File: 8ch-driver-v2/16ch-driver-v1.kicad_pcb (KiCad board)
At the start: 4 copper layers, 234 parts, among them J1 Barrel_Jack, J2 Conn_02x16_Odd_Even, Q1 2N7002E, Q10 2N7002E, Q11 2N7002E, Q12 2N7002E, Q13 2N7002E, Q14 2N7002E, Q15 2N7002E, Q16 2N7002E, Q2 2N7002E, Q3 2N7002E, Q4 2N7002E, Q5 2N7002E, Q6 2N7002E, Q7 2N7002E, Q8 2N7002E, Q9 2N7002E, U1 DRV104PWP, U10 DRV104PWP, U11 DRV104PWP, U12 DRV104PWP, U13 DRV104PWP, U14 DRV104PWP, U15 DRV104PWP, U16 DRV104PWP, U17 BD33FC0FP, U18 FT4232H MINI MODULE, U2 DRV104PWP, U3 DRV104PWP, U4 DRV104PWP, U5 DRV104PWP, U6 DRV104PWP, U7 DRV104PWP, U8 DRV104PWP, U9 DRV104PWP

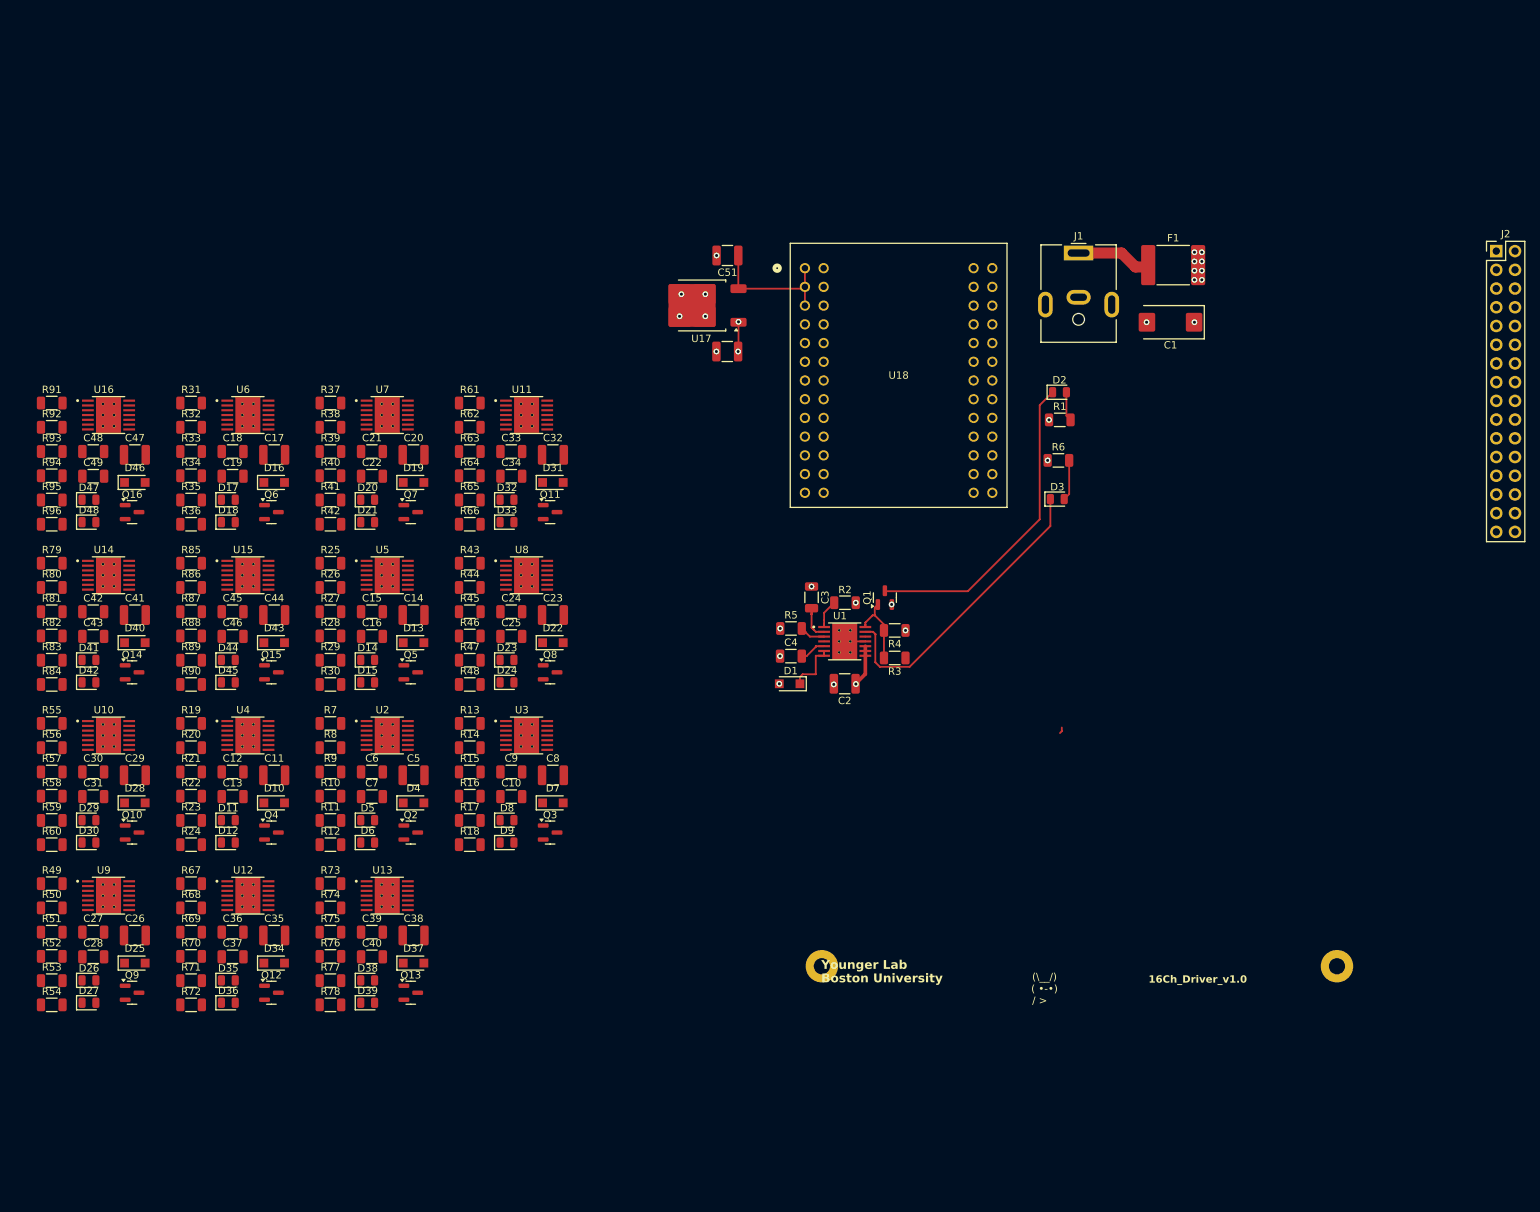
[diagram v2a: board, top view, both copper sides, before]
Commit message: 16-valve PCB layout for inspection
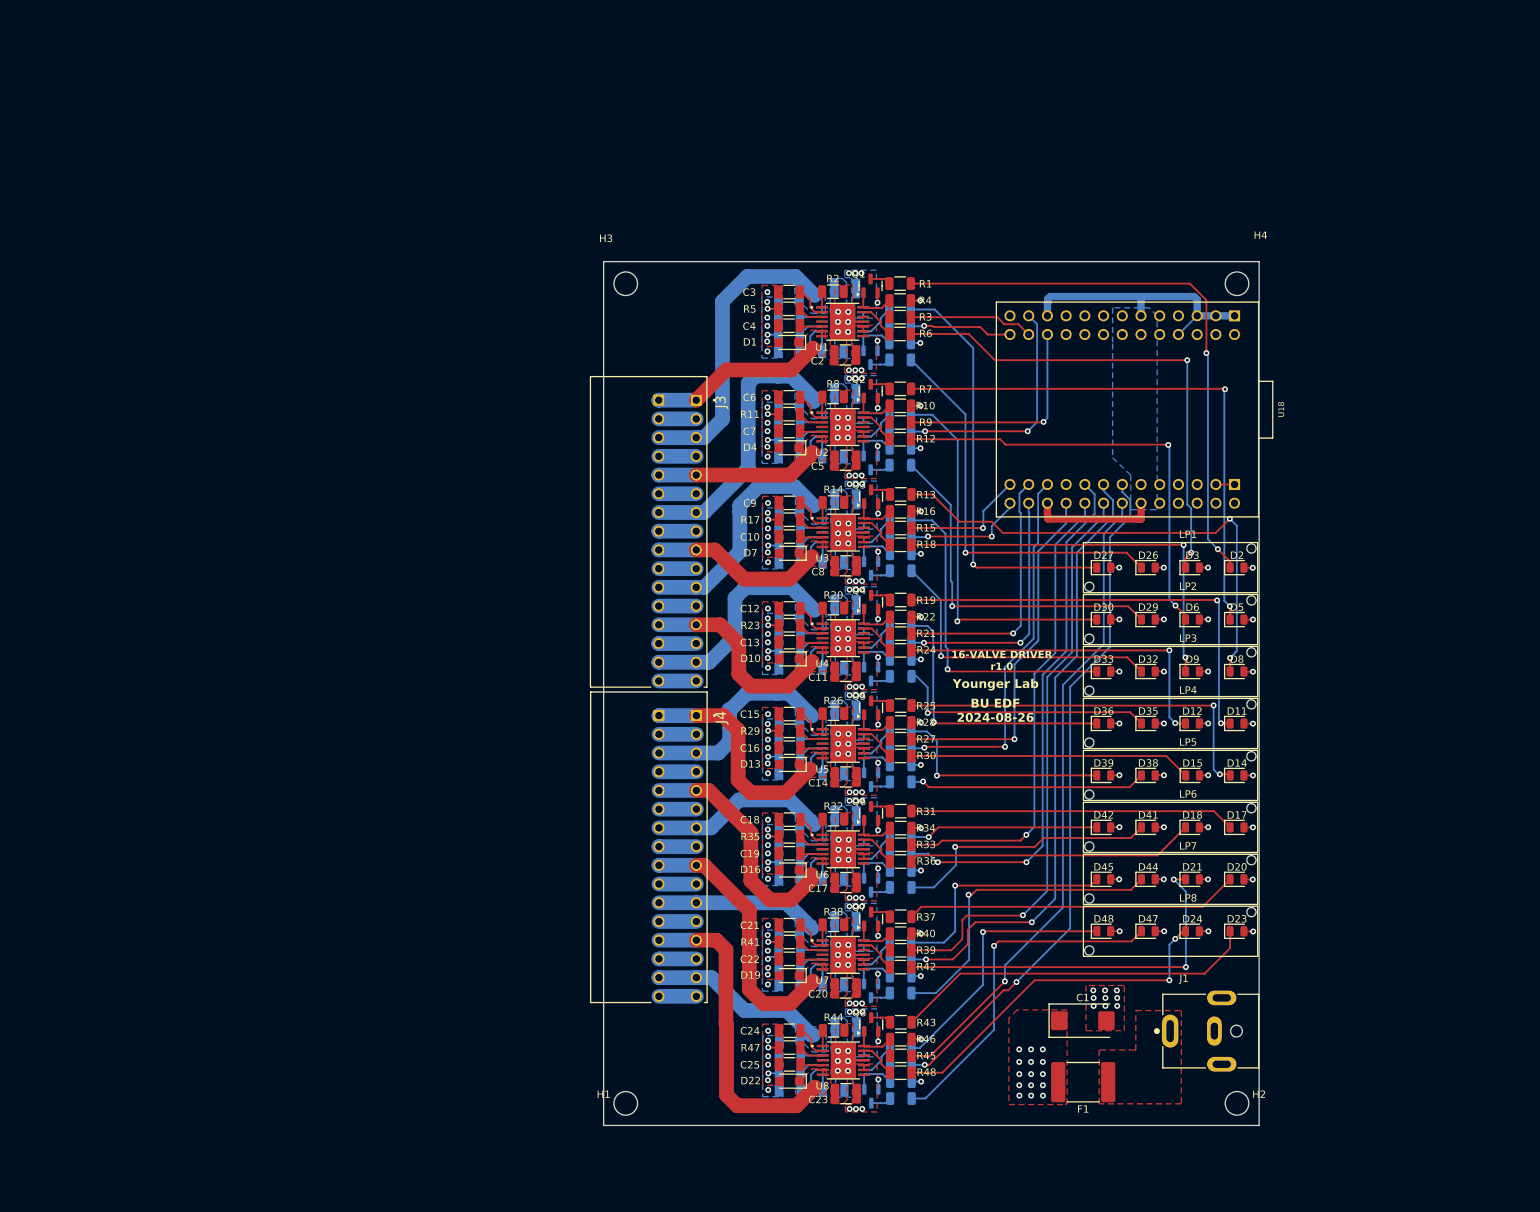
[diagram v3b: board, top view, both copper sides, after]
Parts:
- removed C50, C51: 10uF, Capacitor_SMD:C_1210_3225Metric
- removed J2: Conn_02x16_Odd_Even, Connector_PinHeader_2.54mm:PinHeader_2x16_P2.54mm_Vertical
- removed U17: BD33FC0FP, Package_TO_SOT_SMD:TO-252-2
- added H3: MountingHole, MountingHole:MountingHole_3.2mm_M3, F.Cu at (94.1, 41.8)
- added H4: MountingHole, MountingHole:MountingHole_3.2mm_M3, F.Cu at (183.0, 41.8)
- added J3: TBL009-254-16GY-2GY, footprint:CUI_TBL009-254-16GY-2GY, F.Cu at (106.6, 60.6)
- added J4: TBL009-254-16GY-2GY, footprint:CUI_TBL009-254-16GY-2GY, F.Cu at (106.7, 103.4)
- added LP1: LPF-C014301S, footprint:Lightpipe_LPF-C014301S, F.Cu at (182.7, 83.4)
- added LP2: LPF-C014301S, footprint:Lightpipe_LPF-C014301S, F.Cu at (182.7, 90.4)
- added LP3: LPF-C014301S, footprint:Lightpipe_LPF-C014301S, F.Cu at (182.7, 97.5)
- added LP4: LPF-C014301S, footprint:Lightpipe_LPF-C014301S, F.Cu at (182.7, 104.5)
- added LP5: LPF-C014301S, footprint:Lightpipe_LPF-C014301S, F.Cu at (182.7, 111.6)
- added LP6: LPF-C014301S, footprint:Lightpipe_LPF-C014301S, F.Cu at (182.7, 118.6)
- added LP7: LPF-C014301S, footprint:Lightpipe_LPF-C014301S, F.Cu at (182.7, 125.7)
- added LP8: LPF-C014301S, footprint:Lightpipe_LPF-C014301S, F.Cu at (182.7, 132.7)
- C26, C27, C28, C29, C30, C31, C32, C33, C34, C35, C36, C37, C38, C39, C40, C41, C42, C43, C44, C45, C46, C47, C48, C49, D25, D28, D31, D34, D37, D40, D43, D46, Q10, Q11, Q12, Q13, Q14, Q15, Q16, Q9, R50, R51, R52, R53, R54, R56, R57, R58, R59, R60, R62, R63, R64, R65, R66, R68, R69, R70, R71, R72, R74, R75, R76, R77, R78, R80, R81, R82, R83, R84, R86, R87, R88, R89, R90, R92, R93, R94, R95, R96: moved to B.Cu
- H1, H2: footprint MountingHole:MountingHole_2.2mm_M2_Pad -> MountingHole:MountingHole_3.2mm_M3
- J1: value Barrel_Jack -> PJ-063AH; footprint Connector_BarrelJack:BarrelJack_CUI_PJ-063AH_Horizontal -> footprint:CUI_PJ-063AH
- R1, R13, R19, R25, R31, R37, R43, R7: value 10K -> 4k7
- R49, R55, R61, R67, R73, R79, R85, R91: value 10K -> 4k7; moved to B.Cu
- U1, U2, U3, U4, U5, U6, U7, U8: footprint Solenoid_Driver:IC_TPS27S100BPWPR -> footprint:IC_TPS27S100BPWPR
- U10, U11, U12, U13, U14, U15, U16, U9: footprint Solenoid_Driver:IC_TPS27S100BPWPR -> footprint:IC_TPS27S100BPWPR; moved to B.Cu
- U18: footprint Solenoid_Driver:FT4232H_FTD -> footprint:FT4232H_MINI_MODULE
- moved D47 155.2 mm to (168.0, 132.7)
- moved D26 154.3 mm to (168.0, 83.4)
- moved D27 149.8 mm to (161.9, 83.4)
- moved R91 149.0 mm to (134.4, 155.4), turned to 180 degrees
- moved R54 148.8 mm to (134.3, 48.3), turned to 180 degrees
- moved D48 148.5 mm to (161.9, 132.7)
- moved D29 146.3 mm to (168.0, 90.4)
- moved D41 145.5 mm to (168.0, 118.6)
- moved D17 143.9 mm to (180.0, 118.6)
- moved R93 142.2 mm to (134.4, 150.8), turned to 180 degrees
- moved R52 142.1 mm to (134.3, 52.9), turned to 180 degrees
- moved R94 141.6 mm to (134.4, 153.1), turned to 180 degrees
- moved R51 141.5 mm to (134.3, 50.6), turned to 180 degrees
- moved D30 141.0 mm to (161.9, 90.4)
- moved R92 139.1 mm to (125.3, 154.3), turned to 180 degrees
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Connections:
- net /SpikeAndHoldDriverAndLEDs-1/delay renamed Net-(U1-DELAY_ADJ)
- net /SpikeAndHoldDriverAndLEDs-1/duty renamed Net-(U1-DUTY_CYCLE_ADJ)
- net /SpikeAndHoldDriverAndLEDs-1/freq renamed Net-(U1-OSC_FREQ_ADJ)
- net /SpikeAndHoldDriverAndLEDs-10/delay renamed Net-(U10-DELAY_ADJ)
- net /SpikeAndHoldDriverAndLEDs-10/duty renamed Net-(U10-DUTY_CYCLE_ADJ)
- net /SpikeAndHoldDriverAndLEDs-10/freq renamed Net-(U10-OSC_FREQ_ADJ)
- net /SpikeAndHoldDriverAndLEDs-11/delay renamed Net-(U11-DELAY_ADJ)
- net /SpikeAndHoldDriverAndLEDs-11/duty renamed Net-(U11-DUTY_CYCLE_ADJ)
- net /SpikeAndHoldDriverAndLEDs-11/freq renamed Net-(U11-OSC_FREQ_ADJ)
- net /SpikeAndHoldDriverAndLEDs-12/delay renamed Net-(U12-DELAY_ADJ)
- net /SpikeAndHoldDriverAndLEDs-12/duty renamed Net-(U12-DUTY_CYCLE_ADJ)
- net /SpikeAndHoldDriverAndLEDs-12/freq renamed Net-(U12-OSC_FREQ_ADJ)
- net /SpikeAndHoldDriverAndLEDs-13/delay renamed Net-(U13-DELAY_ADJ)
- net /SpikeAndHoldDriverAndLEDs-13/duty renamed Net-(U13-DUTY_CYCLE_ADJ)
- net /SpikeAndHoldDriverAndLEDs-13/freq renamed Net-(U13-OSC_FREQ_ADJ)
- net /SpikeAndHoldDriverAndLEDs-14/delay renamed Net-(U14-DELAY_ADJ)
- net /SpikeAndHoldDriverAndLEDs-14/duty renamed Net-(U14-DUTY_CYCLE_ADJ)
- net /SpikeAndHoldDriverAndLEDs-14/freq renamed Net-(U14-OSC_FREQ_ADJ)
- net /SpikeAndHoldDriverAndLEDs-15/delay renamed Net-(U15-DELAY_ADJ)
- net /SpikeAndHoldDriverAndLEDs-15/duty renamed Net-(U15-DUTY_CYCLE_ADJ)
- net /SpikeAndHoldDriverAndLEDs-15/freq renamed Net-(U15-OSC_FREQ_ADJ)
- net /SpikeAndHoldDriverAndLEDs-16/delay renamed Net-(U16-DELAY_ADJ)
- net /SpikeAndHoldDriverAndLEDs-16/duty renamed Net-(U16-DUTY_CYCLE_ADJ)
- net /SpikeAndHoldDriverAndLEDs-16/freq renamed Net-(U16-OSC_FREQ_ADJ)
- net /SpikeAndHoldDriverAndLEDs-2/delay renamed Net-(U2-DELAY_ADJ)
- net /SpikeAndHoldDriverAndLEDs-2/duty renamed Net-(U2-DUTY_CYCLE_ADJ)
- net /SpikeAndHoldDriverAndLEDs-2/freq renamed Net-(U2-OSC_FREQ_ADJ)
- net /SpikeAndHoldDriverAndLEDs-3/delay renamed Net-(U3-DELAY_ADJ)
- net /SpikeAndHoldDriverAndLEDs-3/duty renamed Net-(U3-DUTY_CYCLE_ADJ)
- net /SpikeAndHoldDriverAndLEDs-3/freq renamed Net-(U3-OSC_FREQ_ADJ)
- net /SpikeAndHoldDriverAndLEDs-4/delay renamed Net-(U4-DELAY_ADJ)
- net /SpikeAndHoldDriverAndLEDs-4/duty renamed Net-(U4-DUTY_CYCLE_ADJ)
- net /SpikeAndHoldDriverAndLEDs-4/freq renamed Net-(U4-OSC_FREQ_ADJ)
- net /SpikeAndHoldDriverAndLEDs-5/delay renamed Net-(U5-DELAY_ADJ)
- net /SpikeAndHoldDriverAndLEDs-5/duty renamed Net-(U5-DUTY_CYCLE_ADJ)
- net /SpikeAndHoldDriverAndLEDs-5/freq renamed Net-(U5-OSC_FREQ_ADJ)
- net /SpikeAndHoldDriverAndLEDs-6/delay renamed Net-(U6-DELAY_ADJ)
- net /SpikeAndHoldDriverAndLEDs-6/duty renamed Net-(U6-DUTY_CYCLE_ADJ)
- net /SpikeAndHoldDriverAndLEDs-6/freq renamed Net-(U6-OSC_FREQ_ADJ)
- net /SpikeAndHoldDriverAndLEDs-7/delay renamed Net-(U7-DELAY_ADJ)
- net /SpikeAndHoldDriverAndLEDs-7/duty renamed Net-(U7-DUTY_CYCLE_ADJ)
- net /SpikeAndHoldDriverAndLEDs-7/freq renamed Net-(U7-OSC_FREQ_ADJ)
- net /SpikeAndHoldDriverAndLEDs-8/delay renamed Net-(U8-DELAY_ADJ)
- net /SpikeAndHoldDriverAndLEDs-8/duty renamed Net-(U8-DUTY_CYCLE_ADJ)
- net /SpikeAndHoldDriverAndLEDs-8/freq renamed Net-(U8-OSC_FREQ_ADJ)
- net /SpikeAndHoldDriverAndLEDs-9/delay renamed Net-(U9-DELAY_ADJ)
- net /SpikeAndHoldDriverAndLEDs-9/duty renamed Net-(U9-DUTY_CYCLE_ADJ)
- net /SpikeAndHoldDriverAndLEDs-9/freq renamed Net-(U9-OSC_FREQ_ADJ)
- D11 pad 2: Net-(D11-A) -> +12V
- D12 pad 1: /SpikeAndHoldDriverAndLEDs-4/fault -> Net-(D12-K)
- D12 pad 2: Net-(D12-A) -> +12V
- D14 pad 2: Net-(D14-A) -> +12V
- D15 pad 1: /SpikeAndHoldDriverAndLEDs-5/fault -> Net-(D15-K)
- D15 pad 2: Net-(D15-A) -> +12V
- D17 pad 2: Net-(D17-A) -> +12V
- D18 pad 1: /SpikeAndHoldDriverAndLEDs-6/fault -> Net-(D18-K)
- D18 pad 2: Net-(D18-A) -> +12V
- D2 pad 2: Net-(D2-A) -> +12V
- D20 pad 2: Net-(D20-A) -> +12V
- D21 pad 1: /SpikeAndHoldDriverAndLEDs-7/fault -> Net-(D21-K)
- D21 pad 2: Net-(D21-A) -> +12V
- D23 pad 2: Net-(D23-A) -> +12V
- D24 pad 1: /SpikeAndHoldDriverAndLEDs-8/fault -> Net-(D24-K)
- D24 pad 2: Net-(D24-A) -> +12V
- D26 pad 2: Net-(D26-A) -> +12V
- D27 pad 1: /SpikeAndHoldDriverAndLEDs-9/fault -> Net-(D27-K)
- D27 pad 2: Net-(D27-A) -> +12V
- D29 pad 2: Net-(D29-A) -> +12V
- D3 pad 1: /SpikeAndHoldDriverAndLEDs-1/fault -> Net-(D3-K)
- D3 pad 2: Net-(D3-A) -> +12V
- D30 pad 1: /SpikeAndHoldDriverAndLEDs-10/fault -> Net-(D30-K)
- D30 pad 2: Net-(D30-A) -> +12V
- D32 pad 2: Net-(D32-A) -> +12V
- D33 pad 1: /SpikeAndHoldDriverAndLEDs-11/fault -> Net-(D33-K)
- D33 pad 2: Net-(D33-A) -> +12V
- D35 pad 2: Net-(D35-A) -> +12V
- D36 pad 1: /SpikeAndHoldDriverAndLEDs-12/fault -> Net-(D36-K)
- D36 pad 2: Net-(D36-A) -> +12V
- D38 pad 2: Net-(D38-A) -> +12V
- D39 pad 1: /SpikeAndHoldDriverAndLEDs-13/fault -> Net-(D39-K)
- D39 pad 2: Net-(D39-A) -> +12V
- D41 pad 2: Net-(D41-A) -> +12V
- D42 pad 1: /SpikeAndHoldDriverAndLEDs-14/fault -> Net-(D42-K)
- D42 pad 2: Net-(D42-A) -> +12V
- D44 pad 2: Net-(D44-A) -> +12V
- D45 pad 1: /SpikeAndHoldDriverAndLEDs-15/fault -> Net-(D45-K)
- D45 pad 2: Net-(D45-A) -> +12V
- D47 pad 2: Net-(D47-A) -> +12V
- D48 pad 1: /SpikeAndHoldDriverAndLEDs-16/fault -> Net-(D48-K)
- D48 pad 2: Net-(D48-A) -> +12V
- D5 pad 2: Net-(D5-A) -> +12V
- D6 pad 1: /SpikeAndHoldDriverAndLEDs-2/fault -> Net-(D6-K)
- D6 pad 2: Net-(D6-A) -> +12V
- D8 pad 2: Net-(D8-A) -> +12V
- D9 pad 1: /SpikeAndHoldDriverAndLEDs-3/fault -> Net-(D9-K)
- D9 pad 2: Net-(D9-A) -> +12V
- Q1 pad 3: Net-(D2-K) -> Net-(Q1-D)
- Q10 pad 3: Net-(D29-K) -> Net-(Q10-D)
- Q11 pad 3: Net-(D32-K) -> Net-(Q11-D)
- Q12 pad 3: Net-(D35-K) -> Net-(Q12-D)
- Q13 pad 3: Net-(D38-K) -> Net-(Q13-D)
- Q14 pad 3: Net-(D41-K) -> Net-(Q14-D)
- Q15 pad 3: Net-(D44-K) -> Net-(Q15-D)
- Q16 pad 3: Net-(D47-K) -> Net-(Q16-D)
- Q2 pad 3: Net-(D5-K) -> Net-(Q2-D)
- Q3 pad 3: Net-(D8-K) -> Net-(Q3-D)
- Q4 pad 3: Net-(D11-K) -> Net-(Q4-D)
- Q5 pad 3: Net-(D14-K) -> Net-(Q5-D)
- Q6 pad 3: Net-(D17-K) -> Net-(Q6-D)
- Q7 pad 3: Net-(D20-K) -> Net-(Q7-D)
- Q8 pad 3: Net-(D23-K) -> Net-(Q8-D)
- Q9 pad 3: Net-(D26-K) -> Net-(Q9-D)
- R1 pad 1: +12V -> Net-(D2-K)
- R1 pad 2: Net-(D2-A) -> Net-(Q1-D)
- R12 pad 1: +12V -> Net-(D6-K)
- R12 pad 2: Net-(D6-A) -> Net-(U2-STATUS_OK_FLAG)
- R13 pad 1: +12V -> Net-(D8-K)
- R13 pad 2: Net-(D8-A) -> Net-(Q3-D)
- R18 pad 1: +12V -> Net-(D9-K)
- R18 pad 2: Net-(D9-A) -> Net-(U3-STATUS_OK_FLAG)
- R19 pad 1: +12V -> Net-(D11-K)
- R19 pad 2: Net-(D11-A) -> Net-(Q4-D)
- R24 pad 1: +12V -> Net-(D12-K)
- R24 pad 2: Net-(D12-A) -> Net-(U4-STATUS_OK_FLAG)
- R25 pad 1: +12V -> Net-(D14-K)
- R25 pad 2: Net-(D14-A) -> Net-(Q5-D)
- R30 pad 1: +12V -> Net-(D15-K)
- R30 pad 2: Net-(D15-A) -> Net-(U5-STATUS_OK_FLAG)
- R31 pad 1: +12V -> Net-(D17-K)
- R31 pad 2: Net-(D17-A) -> Net-(Q6-D)
- R36 pad 1: +12V -> Net-(D18-K)
- R36 pad 2: Net-(D18-A) -> Net-(U6-STATUS_OK_FLAG)
- R37 pad 1: +12V -> Net-(D20-K)
- R37 pad 2: Net-(D20-A) -> Net-(Q7-D)
- R42 pad 1: +12V -> Net-(D21-K)
- R42 pad 2: Net-(D21-A) -> Net-(U7-STATUS_OK_FLAG)
- R43 pad 1: +12V -> Net-(D23-K)
- R43 pad 2: Net-(D23-A) -> Net-(Q8-D)
- R48 pad 1: +12V -> Net-(D24-K)
- R48 pad 2: Net-(D24-A) -> Net-(U8-STATUS_OK_FLAG)
- R49 pad 1: +12V -> Net-(D26-K)
- R49 pad 2: Net-(D26-A) -> Net-(Q9-D)
- R54 pad 1: +12V -> Net-(D27-K)
- R54 pad 2: Net-(D27-A) -> Net-(U9-STATUS_OK_FLAG)
- R55 pad 1: +12V -> Net-(D29-K)
- R55 pad 2: Net-(D29-A) -> Net-(Q10-D)
- R6 pad 1: +12V -> Net-(D3-K)
- R6 pad 2: Net-(D3-A) -> Net-(U1-STATUS_OK_FLAG)
- R60 pad 1: +12V -> Net-(D30-K)
- R60 pad 2: Net-(D30-A) -> Net-(U10-STATUS_OK_FLAG)
- R61 pad 1: +12V -> Net-(D32-K)
- R61 pad 2: Net-(D32-A) -> Net-(Q11-D)
- R66 pad 1: +12V -> Net-(D33-K)
- R66 pad 2: Net-(D33-A) -> Net-(U11-STATUS_OK_FLAG)
- R67 pad 1: +12V -> Net-(D35-K)
- R67 pad 2: Net-(D35-A) -> Net-(Q12-D)
- R7 pad 1: +12V -> Net-(D5-K)
- R7 pad 2: Net-(D5-A) -> Net-(Q2-D)
- R72 pad 1: +12V -> Net-(D36-K)
- R72 pad 2: Net-(D36-A) -> Net-(U12-STATUS_OK_FLAG)
- R73 pad 1: +12V -> Net-(D38-K)
- R73 pad 2: Net-(D38-A) -> Net-(Q13-D)
- R78 pad 1: +12V -> Net-(D39-K)
- R78 pad 2: Net-(D39-A) -> Net-(U13-STATUS_OK_FLAG)
- R79 pad 1: +12V -> Net-(D41-K)
- R79 pad 2: Net-(D41-A) -> Net-(Q14-D)
- R84 pad 1: +12V -> Net-(D42-K)
- R84 pad 2: Net-(D42-A) -> Net-(U14-STATUS_OK_FLAG)
- R85 pad 1: +12V -> Net-(D44-K)
- R85 pad 2: Net-(D44-A) -> Net-(Q15-D)
- R90 pad 1: +12V -> Net-(D45-K)
- R90 pad 2: Net-(D45-A) -> Net-(U15-STATUS_OK_FLAG)
- R91 pad 1: +12V -> Net-(D47-K)
- R91 pad 2: Net-(D47-A) -> Net-(Q16-D)
- R96 pad 1: +12V -> Net-(D48-K)
- R96 pad 2: Net-(D48-A) -> Net-(U16-STATUS_OK_FLAG)
- U1 pad 13: /SpikeAndHoldDriverAndLEDs-1/fault -> Net-(U1-STATUS_OK_FLAG)
- U10 pad 13: /SpikeAndHoldDriverAndLEDs-10/fault -> Net-(U10-STATUS_OK_FLAG)
- U11 pad 13: /SpikeAndHoldDriverAndLEDs-11/fault -> Net-(U11-STATUS_OK_FLAG)
- U12 pad 13: /SpikeAndHoldDriverAndLEDs-12/fault -> Net-(U12-STATUS_OK_FLAG)
- U13 pad 13: /SpikeAndHoldDriverAndLEDs-13/fault -> Net-(U13-STATUS_OK_FLAG)
- U14 pad 13: /SpikeAndHoldDriverAndLEDs-14/fault -> Net-(U14-STATUS_OK_FLAG)
- U15 pad 13: /SpikeAndHoldDriverAndLEDs-15/fault -> Net-(U15-STATUS_OK_FLAG)
- U16 pad 13: /SpikeAndHoldDriverAndLEDs-16/fault -> Net-(U16-STATUS_OK_FLAG)
- U18 pad CN2-10: /SpikeAndHoldDriverAndLEDs-2/TTLInput -> unconnected-(U18-AD1-PadCN2-10)
- U18 pad CN2-11: unconnected-(U18-VIO-PadCN2-11) -> +3.3V
- U18 pad CN2-12: /SpikeAndHoldDriverAndLEDs-4/TTLInput -> unconnected-(U18-AD3-PadCN2-12)
- U18 pad CN2-13: /SpikeAndHoldDriverAndLEDs-6/TTLInput -> unconnected-(U18-AD5-PadCN2-13)
- U18 pad CN2-14: /SpikeAndHoldDriverAndLEDs-5/TTLInput -> unconnected-(U18-AD4-PadCN2-14)
- U18 pad CN2-15: /SpikeAndHoldDriverAndLEDs-8/TTLInput -> unconnected-(U18-AD7-PadCN2-15)
- U18 pad CN2-16: /SpikeAndHoldDriverAndLEDs-7/TTLInput -> unconnected-(U18-AD6-PadCN2-16)
- U18 pad CN2-21: unconnected-(U18-VIO-PadCN2-21) -> +3.3V
- U18 pad CN2-22: unconnected-(U18-BD4-PadCN2-22) -> /SpikeAndHoldDriverAndLEDs-2/TTLInput
- U18 pad CN2-23: unconnected-(U18-BD6-PadCN2-23) -> /SpikeAndHoldDriverAndLEDs-10/TTLInput
- U18 pad CN2-24: unconnected-(U18-BD5-PadCN2-24) -> /SpikeAndHoldDriverAndLEDs-1/TTLInput
- U18 pad CN2-26: unconnected-(U18-BD7-PadCN2-26) -> /SpikeAndHoldDriverAndLEDs-9/TTLInput
- U18 pad CN2-7: /SpikeAndHoldDriverAndLEDs-1/TTLInput -> unconnected-(U18-AD0-PadCN2-7)
- U18 pad CN2-8: unconnected-(U18-RESET#-PadCN2-8) -> +3.3V
- U18 pad CN2-9: /SpikeAndHoldDriverAndLEDs-3/TTLInput -> unconnected-(U18-AD2-PadCN2-9)
- U18 pad CN3-12: unconnected-(U18-VIO-PadCN3-12) -> +3.3V
- U18 pad CN3-13: unconnected-(U18-DD4-PadCN3-13) -> /SpikeAndHoldDriverAndLEDs-16/TTLInput
- U18 pad CN3-14: unconnected-(U18-DD3-PadCN3-14) -> /SpikeAndHoldDriverAndLEDs-8/TTLInput
- U18 pad CN3-15: unconnected-(U18-DD2-PadCN3-15) -> /SpikeAndHoldDriverAndLEDs-15/TTLInput
- U18 pad CN3-16: unconnected-(U18-DD1-PadCN3-16) -> /SpikeAndHoldDriverAndLEDs-7/TTLInput
- U18 pad CN3-17: unconnected-(U18-DD0-PadCN3-17) -> /SpikeAndHoldDriverAndLEDs-14/TTLInput
- U18 pad CN3-18: /SpikeAndHoldDriverAndLEDs-16/TTLInput -> /SpikeAndHoldDriverAndLEDs-6/TTLInput
- U18 pad CN3-19: /SpikeAndHoldDriverAndLEDs-15/TTLInput -> unconnected-(U18-CD6-PadCN3-19)
- U18 pad CN3-20: /SpikeAndHoldDriverAndLEDs-14/TTLInput -> /SpikeAndHoldDriverAndLEDs-5/TTLInput
- U18 pad CN3-22: unconnected-(U18-VIO-PadCN3-22) -> +3.3V
- U18 pad CN3-23: /SpikeAndHoldDriverAndLEDs-12/TTLInput -> /SpikeAndHoldDriverAndLEDs-4/TTLInput
- U18 pad CN3-24: /SpikeAndHoldDriverAndLEDs-11/TTLInput -> /SpikeAndHoldDriverAndLEDs-12/TTLInput
- U18 pad CN3-25: /SpikeAndHoldDriverAndLEDs-10/TTLInput -> /SpikeAndHoldDriverAndLEDs-3/TTLInput
- U18 pad CN3-26: /SpikeAndHoldDriverAndLEDs-9/TTLInput -> /SpikeAndHoldDriverAndLEDs-11/TTLInput
- U2 pad 13: /SpikeAndHoldDriverAndLEDs-2/fault -> Net-(U2-STATUS_OK_FLAG)
- U3 pad 13: /SpikeAndHoldDriverAndLEDs-3/fault -> Net-(U3-STATUS_OK_FLAG)
- U4 pad 13: /SpikeAndHoldDriverAndLEDs-4/fault -> Net-(U4-STATUS_OK_FLAG)
- U5 pad 13: /SpikeAndHoldDriverAndLEDs-5/fault -> Net-(U5-STATUS_OK_FLAG)
- U6 pad 13: /SpikeAndHoldDriverAndLEDs-6/fault -> Net-(U6-STATUS_OK_FLAG)
- U7 pad 13: /SpikeAndHoldDriverAndLEDs-7/fault -> Net-(U7-STATUS_OK_FLAG)
- U8 pad 13: /SpikeAndHoldDriverAndLEDs-8/fault -> Net-(U8-STATUS_OK_FLAG)
- U9 pad 13: /SpikeAndHoldDriverAndLEDs-9/fault -> Net-(U9-STATUS_OK_FLAG)
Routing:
- net GND: track 2.94 -> 179.1 mm, vias 15 -> 153
- net /SpikeAndHoldDriverAndLEDs-16/TTLInput: track 0.00 -> 93.2 mm, vias 0 -> 2
- net /SpikeAndHoldDriverAndLEDs-8/TTLInput: track 0.00 -> 88.3 mm, vias 0 -> 1
- net /SpikeAndHoldDriverAndLEDs-15/TTLInput: track 0.00 -> 84.2 mm, vias 0 -> 2
- net /SpikeAndHoldDriverAndLEDs-7/TTLInput: track 0.00 -> 79.1 mm, vias 0 -> 1
- net Net-(D5-K): track 0.00 -> 74.2 mm, vias 0 -> 2
- net /SpikeAndHoldDriverAndLEDs-14/TTLInput: track 0.00 -> 71.7 mm, vias 0 -> 2
- net Net-(D3-K): track 0.00 -> 67.7 mm, vias 0 -> 2
- net Net-(D8-K): track 0.00 -> 67.7 mm, vias 0 -> 2
- net /SpikeAndHoldDriverAndLEDs-6/TTLInput: track 0.00 -> 64.5 mm, vias 0 -> 1
- net Net-(D6-K): track 0.00 -> 59.9 mm, vias 0 -> 2
- net Net-(D11-K): track 0.00 -> 59.6 mm, vias 0 -> 2
- net Net-(D27-K): track 0.00 -> 57.0 mm, vias 0 -> 1
- net Net-(D9-K): track 0.00 -> 54.2 mm, vias 0 -> 2
- net Net-(D26-K): track 0.00 -> 53.9 mm, vias 0 -> 1
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- added copper zone on B.Cu, net +12V
- added copper zone on F.Cu, net +12V
- added copper zone on In2.Cu, net +12V
- added copper zone on B.Cu, net +3.3V
- added copper zone on F.Cu, net /12V_IN
- added copper zone on F.Cu, net /SpikeAndHoldDriverAndLEDs-1/DriveOut
- added copper zone on B.Cu, net /SpikeAndHoldDriverAndLEDs-10/DriveOut
- added copper zone on B.Cu, net /SpikeAndHoldDriverAndLEDs-11/DriveOut
- added copper zone on B.Cu, net /SpikeAndHoldDriverAndLEDs-12/DriveOut
- added copper zone on B.Cu, net /SpikeAndHoldDriverAndLEDs-13/DriveOut
- added copper zone on B.Cu, net /SpikeAndHoldDriverAndLEDs-14/DriveOut
- added copper zone on B.Cu, net /SpikeAndHoldDriverAndLEDs-15/DriveOut
- added copper zone on B.Cu, net /SpikeAndHoldDriverAndLEDs-16/DriveOut
- added copper zone on F.Cu, net /SpikeAndHoldDriverAndLEDs-2/DriveOut
- added copper zone on F.Cu, net /SpikeAndHoldDriverAndLEDs-3/DriveOut
- added copper zone on F.Cu, net /SpikeAndHoldDriverAndLEDs-4/DriveOut
- added copper zone on F.Cu, net /SpikeAndHoldDriverAndLEDs-5/DriveOut
- added copper zone on F.Cu, net /SpikeAndHoldDriverAndLEDs-6/DriveOut
- added copper zone on F.Cu, net /SpikeAndHoldDriverAndLEDs-7/DriveOut
- added copper zone on F.Cu, net /SpikeAndHoldDriverAndLEDs-8/DriveOut
- added copper zone on B.Cu, net /SpikeAndHoldDriverAndLEDs-9/DriveOut
- added copper zone on B.Cu, net GND
- added copper zone on F.Cu, net GND
- added copper zone on In1.Cu, net GND
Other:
- board outline added: 89 x 117.2 mm
- board text added: "16-VALVE DRIVER r1.0"
- board text added: "BU EDF 2024-08-26"
- board text removed: "(\__/) ( •-•) / >"
- board text removed: "16Ch_Driver_v1.0"
- board text removed: "Boston University"

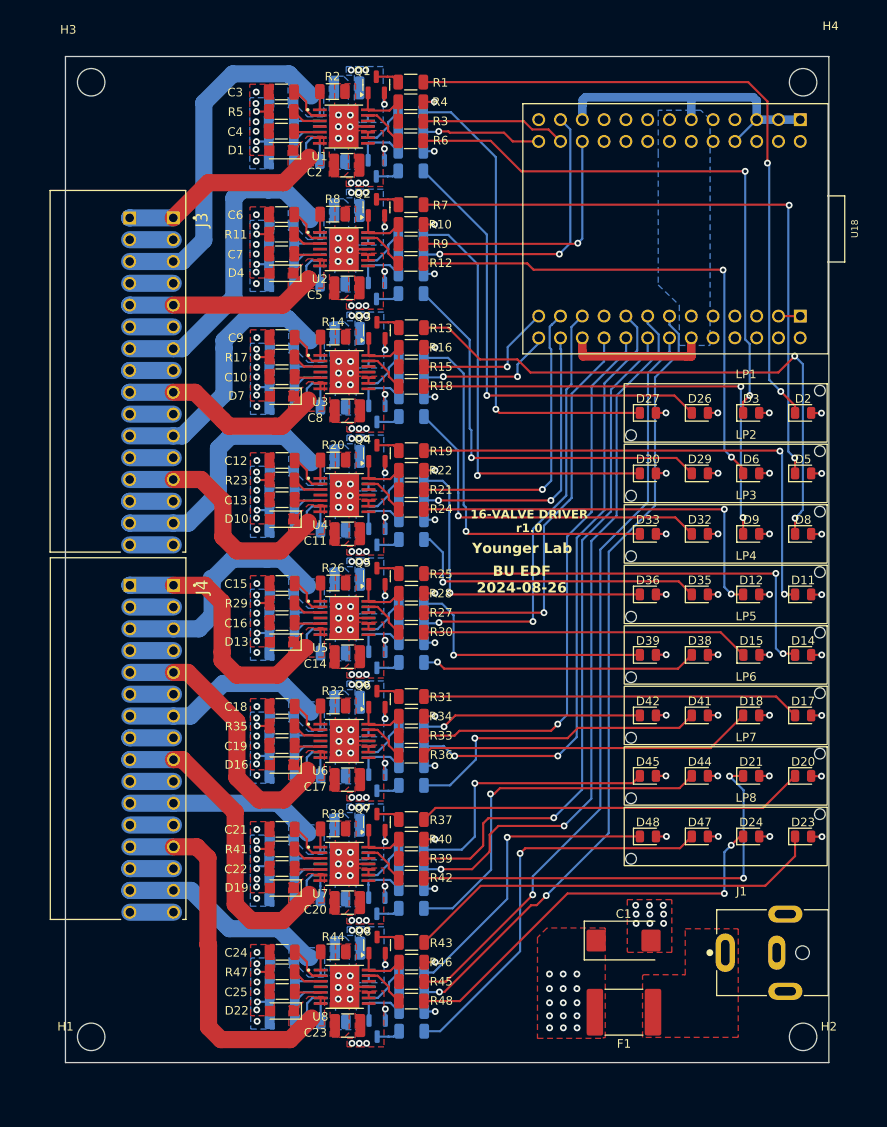
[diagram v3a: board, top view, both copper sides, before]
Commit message: Larger Board and DRC Cleanup
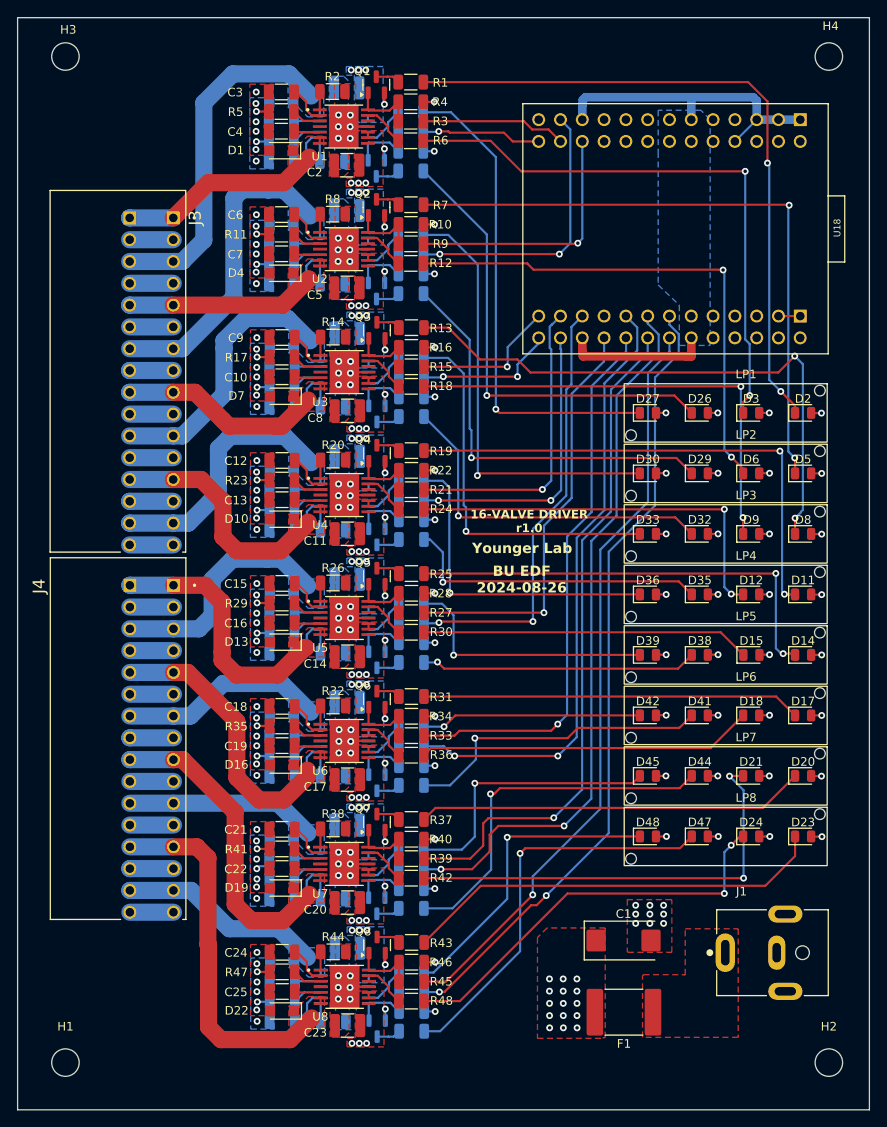
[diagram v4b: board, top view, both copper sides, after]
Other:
- board size 89 x 117.2 mm -> 99.2 x 127.2 mm
